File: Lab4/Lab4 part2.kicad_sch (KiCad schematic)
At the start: 10 parts

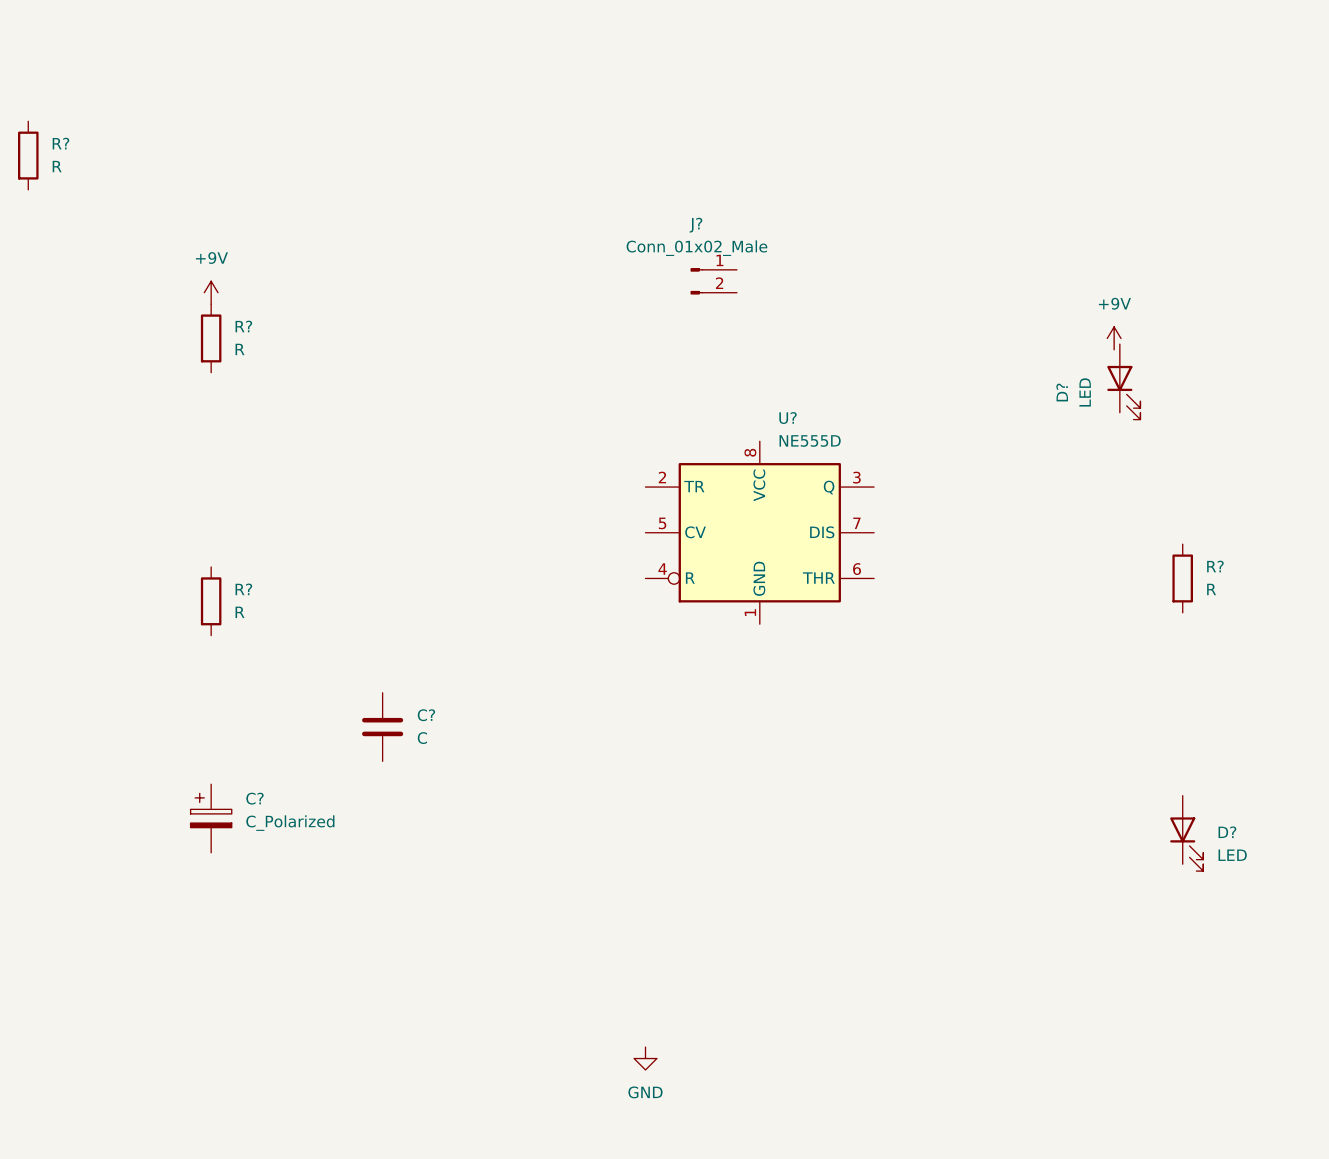
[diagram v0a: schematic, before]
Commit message: Y direction and 2 netlabels update
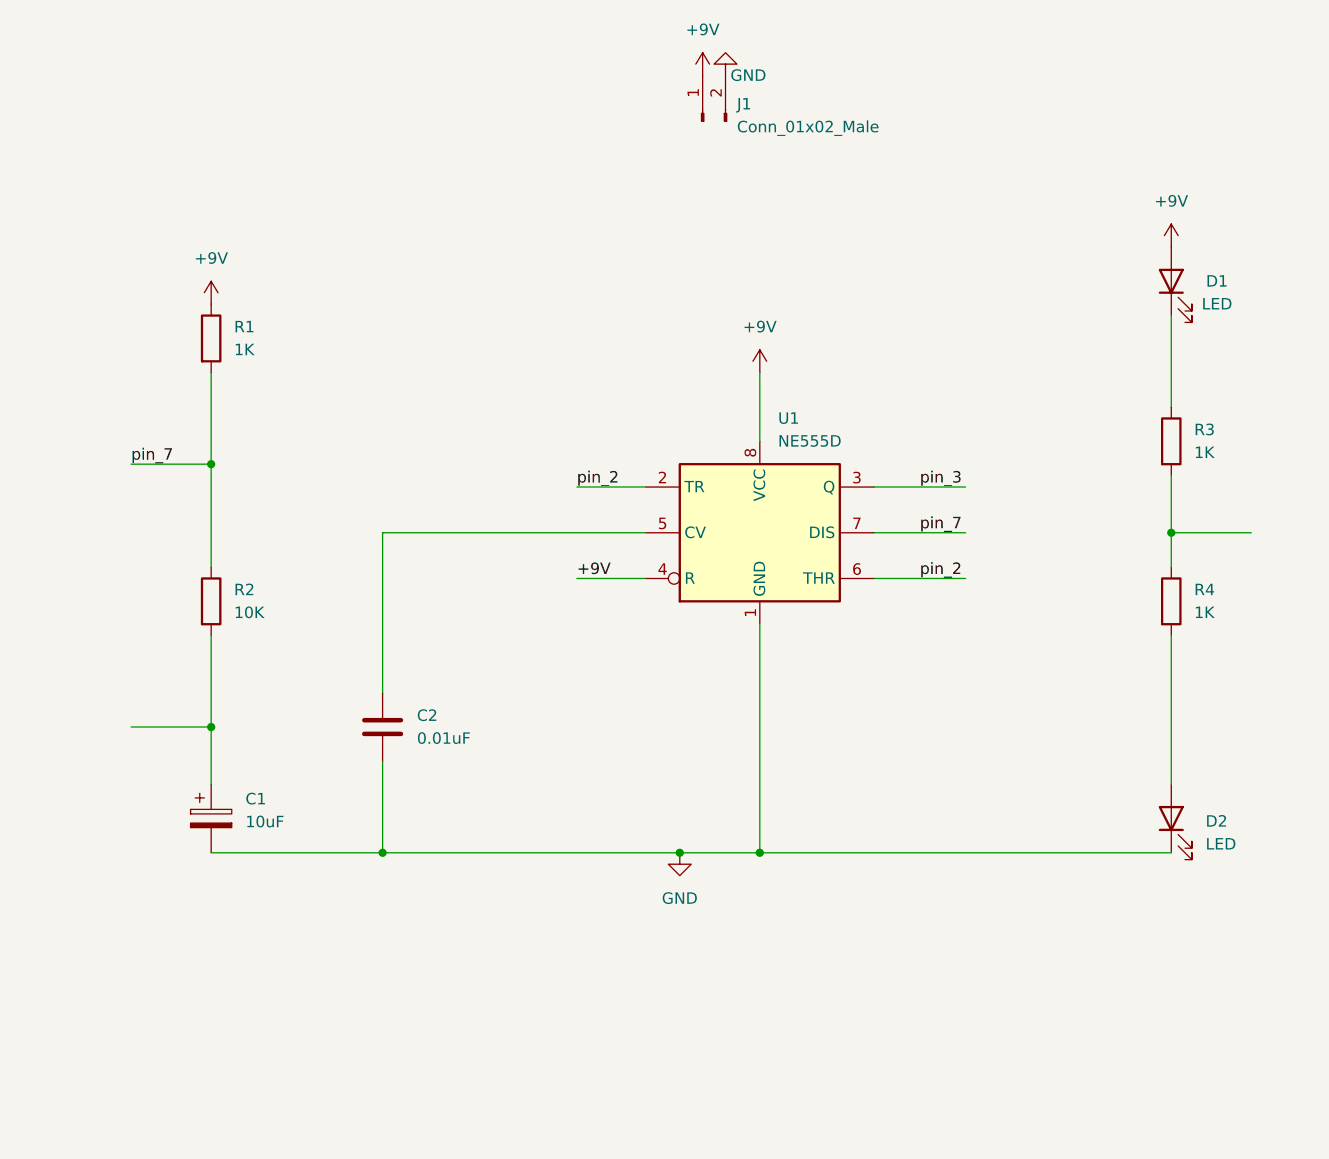
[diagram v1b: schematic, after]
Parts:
- C1: renamed from C?; value C_Polarized -> 10uF
- C2: renamed from C?; value C -> 0.01uF
- R1, R3, R4: renamed from R?; value R -> 1K
- R2: renamed from R?; value R -> 10K
- gave numbers to parts that had none: 4
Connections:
- net +9V: now also D1.2 (A), J1.1 (Pin_1), U1.4 (R), U1.8 (VCC)
- net GND: now also C1.2, C2.2, D2.1 (K), J1.2 (Pin_2), U1.1 (GND)
- net at D2.2 (A): now also R4.2
- net at D1.1 (K): now also R3.1
- net at R4.1: now also R3.2
- net pin_7: now reaches R1.2
- net pin_7: now also R2.1, U1.7 (DIS)
- net pin_2: now reaches U1.2 (TR)
- net pin_2: now also U1.6 (THR)
- net pin_3: now reaches U1.3 (Q)
- net at U1.5 (CV): now also C2.1
- net at C1.1: now also R2.2
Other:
- moved on the sheet: D1, D2, J1, R3, R4

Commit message: Lab5 pictures
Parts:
- added R1, R3, R4: 1K, symbol Device:R
- added R2: 10K, symbol Device:R
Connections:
- net +9V: now also R1.1
- net pin_2: now also C1.1, R2.2, R2.2
- net pin_3: now also R3.2, R4.1, R3.2, R4.1
- net pin_7: now also R1.2, R2.1
